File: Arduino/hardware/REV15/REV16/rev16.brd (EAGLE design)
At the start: 50 x 50 mm, 10 parts, among them U1 TC1185SMD

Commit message: up to rev18 cleaned up
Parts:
- moved - 34.7 mm to (48.6, 32.2), turned to 0 degrees
- moved + 34.2 mm to (48.6, 19.4), turned to 0 degrees
- moved U$2 27.9 mm to (-9.03, 25.8)
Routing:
- net VCC: track 68.2 -> 42.2 mm
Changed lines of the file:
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@@
 <plain>
 <text x="-5.318971875" y="13.33876875" size="1" layer="25" font="vector" rot="R180">20151208</text>
-<text x="24.149196875" y="-4.224378125" size="1" layer="22" font="vector" rot="MR0">License: http://goo.gl/3d71UJ</text>
-<text x="12.333878125" y="-0.70546875" size="1" layer="25" font="vector" rot="R180">OpenTRV.org.uk</text>
-<text x="2.54" y="24.13" size="1" layer="25" rot="R270">Remove jumper
+<text x="13.950803125" y="1.684378125" size="1" layer="22" font="vector" rot="MR180">License: http://goo.gl/3d71UJ</text>
+<text x="19.416121875" y="0.70546875" size="1" layer="25" font="vector">OpenTRV.org.uk</text>
+<text x="2.54" y="24.13" size="1" layer="25" font="vector" rot="R270">Remove jumper
 if battery power</text>
 <wire x1="0" y1="0" x2="0" y2="50" width="0.4064" layer="20"/>
@@
 <wire x1="50" y1="50" x2="50" y2="0" width="0.4064" layer="20"/>
 <wire x1="50" y1="0" x2="0" y2="0" width="0.4064" layer="20"/>
-<hole x="25.37" y="18.585" drill="2.8"/>
+<hole x="31.58" y="25.37" drill="2.8"/>
 </plain>
 <attributes>
@@
 </autorouter>
 <elements>
-<element name="U$2" library="logo" package="TONNE" value="" x="-9.025" y="53.75711875"/>
+<element name="U$2" library="logo" package="TONNE" value="" x="-9.025" y="25.81711875"/>
 <element name="U$1" library="ohw-logo" package="OSHW_10X200_NOTEXT" value="" x="-10.725834375" y="16.02610625"/>
-<element name="-" library="wirepad" package="2,15/1,0" value="" x="32.17" y="1.585" rot="R270"/>
-<element name="+" library="wirepad" package="2,15/1,0" value="" x="19.37" y="1.585" rot="R270"/>
+<element name="-" library="wirepad" package="2,15/1,0" value="" x="48.58" y="32.17"/>
+<element name="+" library="wirepad" package="2,15/1,0" value="" x="48.58" y="19.37"/>
 <element name="USBPOWER" library="micro-usb-fci-10103592" package="MICRO-USB-FCI-10103592" value="MICRO-USB-FCI-10103592" x="3.2" y="34.401771875" rot="MR90"/>
 <element name="I2C_EXT" library="pinhead" package="2X10" value="" x="18.05" y="45.905" smashed="yes">
-<attribute name="NAME" x="23.13" y="41.46" size="1.27" layer="25" ratio="10"/>
+<attribute name="NAME" x="23.13" y="41.46" size="1" layer="25" font="vector"/>
 <attribute name="VALUE" x="5.35" y="41.46" size="1.27" layer="27"/>
 </element>
 <element name="C1" library="SparkFun-Passives" package="0603-CAP" value="10uF 10V" x="11.43" y="31.75" smashed="yes" rot="R180">
-<attribute name="NAME" x="12.954" y="30.353" size="0.4064" layer="25" font="vector" rot="R180"/>
+<attribute name="NAME" x="15.494" y="32.258" size="1" layer="25" font="vector" rot="R180"/>
 </element>
 <element name="C2" library="SparkFun-Passives" package="0603-CAP" value="10uF 10V" x="11.43" y="41.275" smashed="yes" rot="R180">
-<attribute name="NAME" x="12.954" y="39.878" size="0.4064" layer="25" font="vector" rot="R180"/>
+<attribute name="NAME" x="15.494" y="41.783" size="1" layer="25" font="vector" rot="R180"/>
 </element>
 <element name="U1" library="3.3VREG" package="TC1185" value="TC1185SMD" x="11.43" y="36.83" smashed="yes">
-<attribute name="NAME" x="13.589" y="37.084" size="0.4064" layer="25" rot="R270"/>
-</element>
-<element name="JP1" library="jumper" package="JP1" value="" x="3.81" y="27.94"/>
+<attribute name="NAME" x="13.589" y="37.719" size="1" layer="25" font="vector" rot="R270"/>
+</element>
+<element name="JP1" library="jumper" package="JP1" value="" x="3.81" y="27.94" smashed="yes">
+<attribute name="NAME" x="7.112" y="26.67" size="1" layer="25" font="vector" rot="R90"/>
+<attribute name="VALUE" x="6.858" y="25.4" size="1.27" layer="27" ratio="10" rot="R90"/>
+</element>
 </elements>
 <signals>
@@
 <contactref element="JP1" pad="2"/>
 <wire x1="4.572" y1="29.1592" x2="3.8608" y2="29.1592" width="0.4064" layer="1"/>
-<wire x1="17.8816" y1="15.8496" x2="8.4328" y2="25.2984" width="0.4064" layer="1"/>
+<wire x1="34.3154" y1="17.8816" x2="8.4328" y2="25.2984" width="0" layer="19" extent="1-16"/>
 <wire x1="8.4328" y1="25.2984" x2="4.572" y2="29.1592" width="0.4064" layer="1"/>
-<wire x1="17.8816" y1="3.1496" x2="17.8816" y2="15.8496" width="0.4064" layer="1"/>
-<wire x1="19.4056" y1="1.6256" x2="17.8816" y2="3.1496" width="0.4064" layer="1"/>
+<wire x1="47.0154" y1="17.8816" x2="34.3154" y2="17.8816" width="0" layer="19" extent="1-16"/>
+<wire x1="48.5394" y1="19.4056" x2="47.0154" y2="17.8816" width="0.4064" layer="1"/>
 <wire x1="3.8608" y1="29.1592" x2="3.81" y2="29.21" width="0.4064" layer="1"/>
-<wire x1="19.4056" y1="1.6256" x2="19.37" y2="1.585" width="0.4064" layer="1"/>
+<wire x1="48.5394" y1="19.4056" x2="48.58" y2="19.37" width="0.4064" layer="1"/>
 <wire x1="6.096" y1="47.1424" x2="6.604" y2="47.1424" width="0.4064" layer="1"/>
 <wire x1="4.7752" y1="45.8216" x2="6.096" y2="47.1424" width="0.4064" layer="1"/>

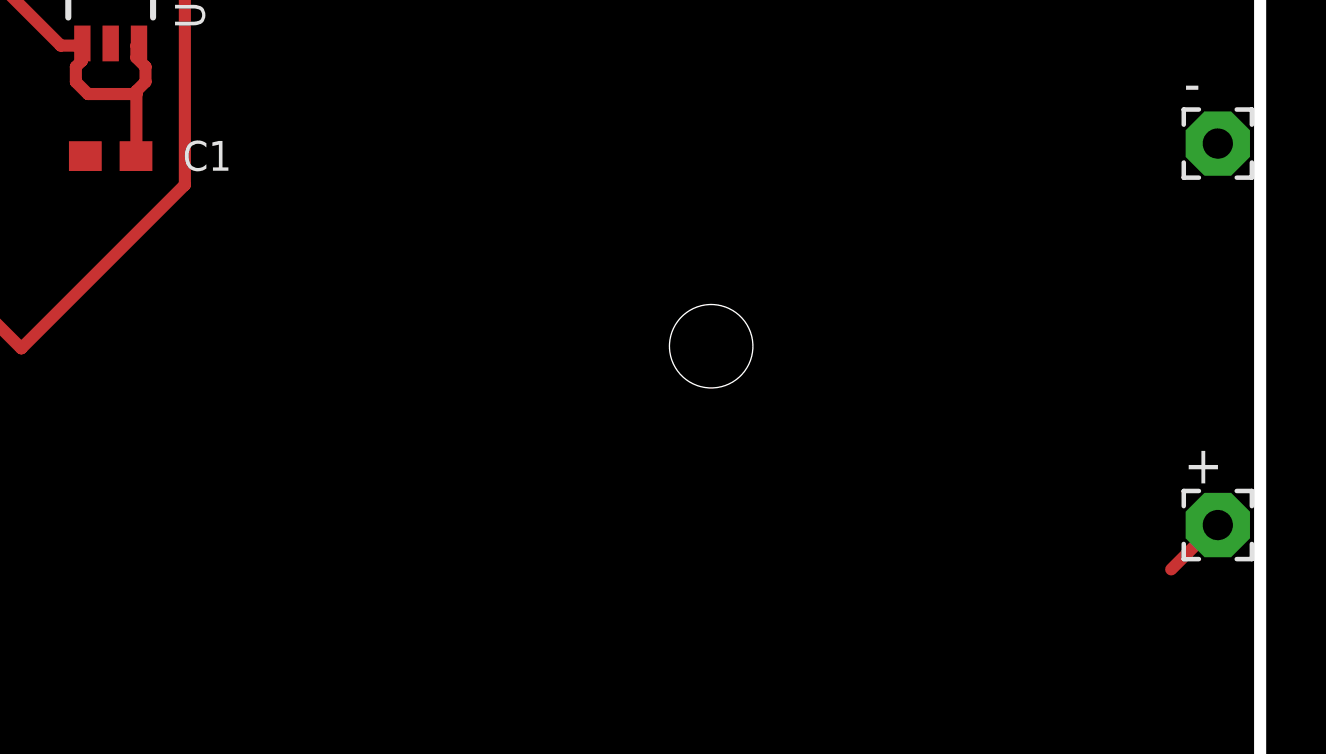
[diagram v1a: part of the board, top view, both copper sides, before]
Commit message: up to rev18 DRC check and ground plane
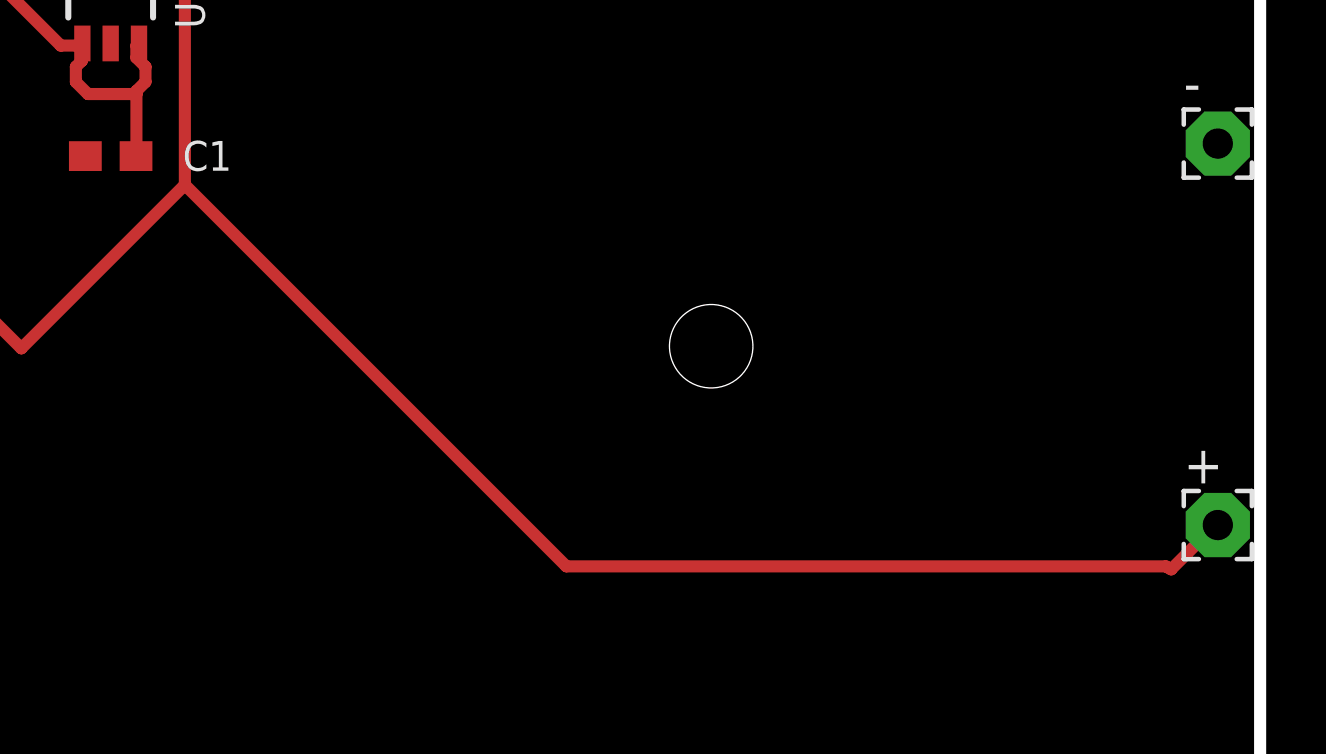
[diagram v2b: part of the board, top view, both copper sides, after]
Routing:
- net VCC: track 42.2 -> 80.6 mm
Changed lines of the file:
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@@
 <contactref element="JP1" pad="2"/>
 <wire x1="4.572" y1="29.1592" x2="3.8608" y2="29.1592" width="0.4064" layer="1"/>
-<wire x1="34.3154" y1="17.8816" x2="8.4328" y2="25.2984" width="0" layer="19" extent="1-16"/>
 <wire x1="8.4328" y1="25.2984" x2="4.572" y2="29.1592" width="0.4064" layer="1"/>
-<wire x1="47.0154" y1="17.8816" x2="34.3154" y2="17.8816" width="0" layer="19" extent="1-16"/>
 <wire x1="48.5394" y1="19.4056" x2="47.0154" y2="17.8816" width="0.4064" layer="1"/>
 <wire x1="3.8608" y1="29.1592" x2="3.81" y2="29.21" width="0.4064" layer="1"/>
@@
 <wire x1="8.4328" y1="25.2984" x2="13.9192" y2="30.7848" width="0.4064" layer="1"/>
 <wire x1="6.604" y1="47.1424" x2="6.62" y2="47.175" width="0.4064" layer="1"/>
+<wire x1="26.7208" y1="17.9832" x2="46.8376" y2="17.9832" width="0.4064" layer="1"/>
+<wire x1="13.9192" y1="30.7848" x2="26.7208" y2="17.9832" width="0.4064" layer="1"/>
+<wire x1="46.8376" y1="17.9832" x2="47.0154" y2="17.8816" width="0.4064" layer="1"/>
 </signal>
 <signal name="GND" class="1">

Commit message: REV15-18 cleaned up, need sanity check
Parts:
- moved U$2 47.6 mm to (38.0, 33.4)
- moved U$1 24.1 mm to (12.1, 8.41)
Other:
- board text added: "20160229"
- board text removed: "20151208"
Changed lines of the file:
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@@
 <board>
 <plain>
-<text x="-5.318971875" y="13.33876875" size="1" layer="25" font="vector" rot="R180">20151208</text>
+<text x="47.62123125" y="13.731028125" size="1" layer="25" font="vector" rot="R270">20160229</text>
 <text x="13.950803125" y="1.684378125" size="1" layer="22" font="vector" rot="MR180">License: http://goo.gl/3d71UJ</text>
 <text x="19.416121875" y="0.70546875" size="1" layer="25" font="vector">OpenTRV.org.uk</text>
@@
 </autorouter>
 <elements>
-<element name="U$2" library="logo" package="TONNE" value="" x="-9.025" y="25.81711875"/>
-<element name="U$1" library="ohw-logo" package="OSHW_10X200_NOTEXT" value="" x="-10.725834375" y="16.02610625"/>
+<element name="U$2" library="logo" package="TONNE" value="" x="37.965" y="33.43711875"/>
+<element name="U$1" library="ohw-logo" package="OSHW_10X200_NOTEXT" value="" x="12.134165625" y="8.40610625"/>
 <element name="-" library="wirepad" package="2,15/1,0" value="" x="48.58" y="32.17"/>
 <element name="+" library="wirepad" package="2,15/1,0" value="" x="48.58" y="19.37"/>

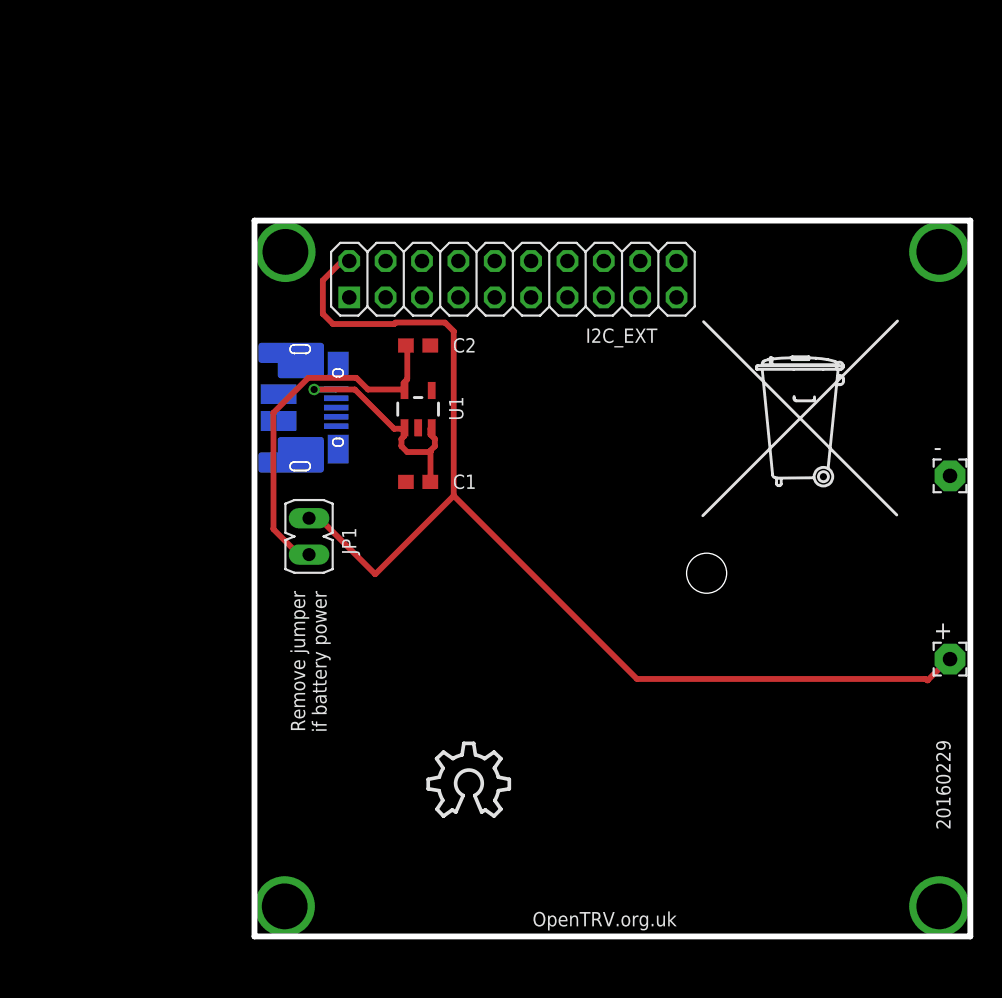
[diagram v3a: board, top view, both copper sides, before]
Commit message: rev15-18 changed as per Deniz suggeastions
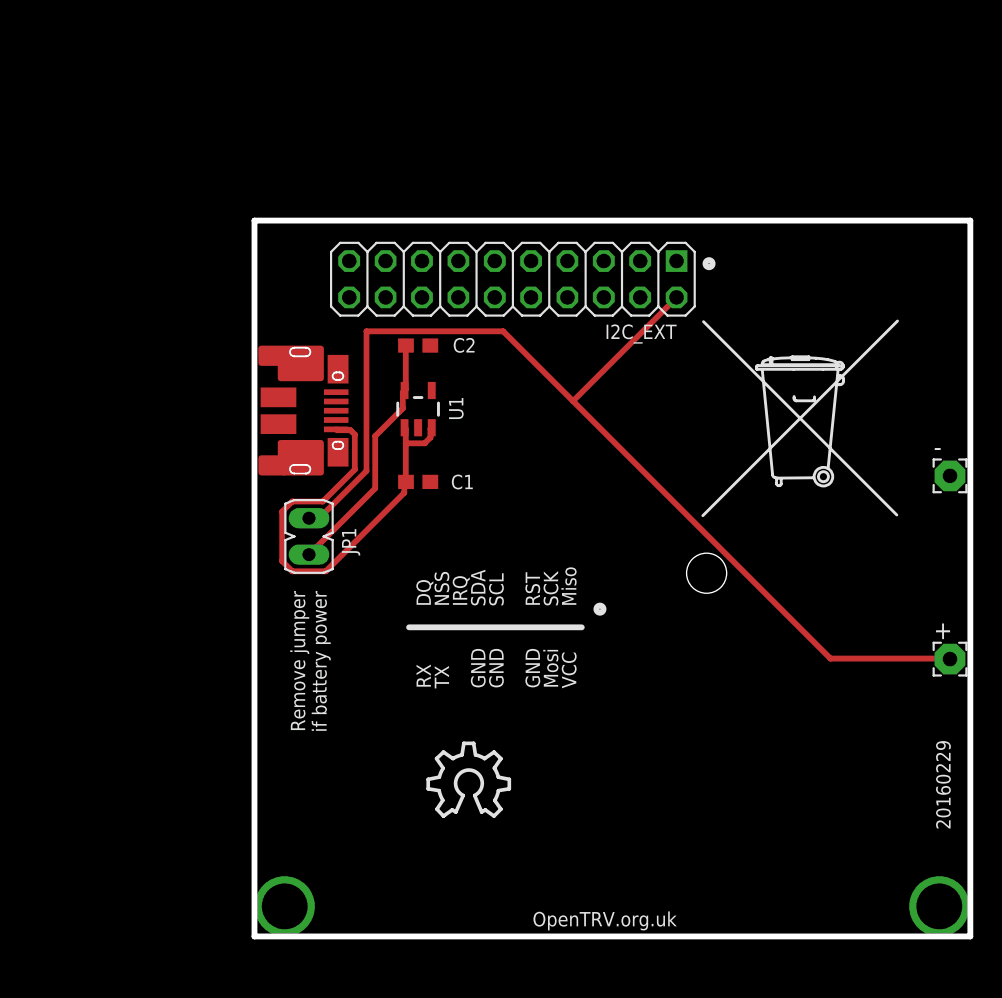
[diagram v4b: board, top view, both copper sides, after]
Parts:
- moved USBPOWER 4.86 mm to (3.20, 39.3), flipped to the top, turned to 270 degrees
- turned C1 to 0 degrees
- turned I2C_EXT to 180 degrees
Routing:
- net 5V: track 16.7 -> 32.0 mm, vias 1 -> 0
- net N$8: track 25.2 -> 17.4 mm
- net VCC: track 80.6 -> 75.6 mm
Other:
- board text added: "DQ"
- board text added: "GND"
- board text added: "IRQ"
- board text added: "Miso"
- board text added: "Mosi"
- board text added: "NSS"
- board text added: "RST"
- board text added: "RX"
- board text added: "SCK"
- board text added: "SCL"
- board text added: "SDA"
- board text added: "TX"
- board text added: "VCC"

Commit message: ic2_ext labels closer to connector
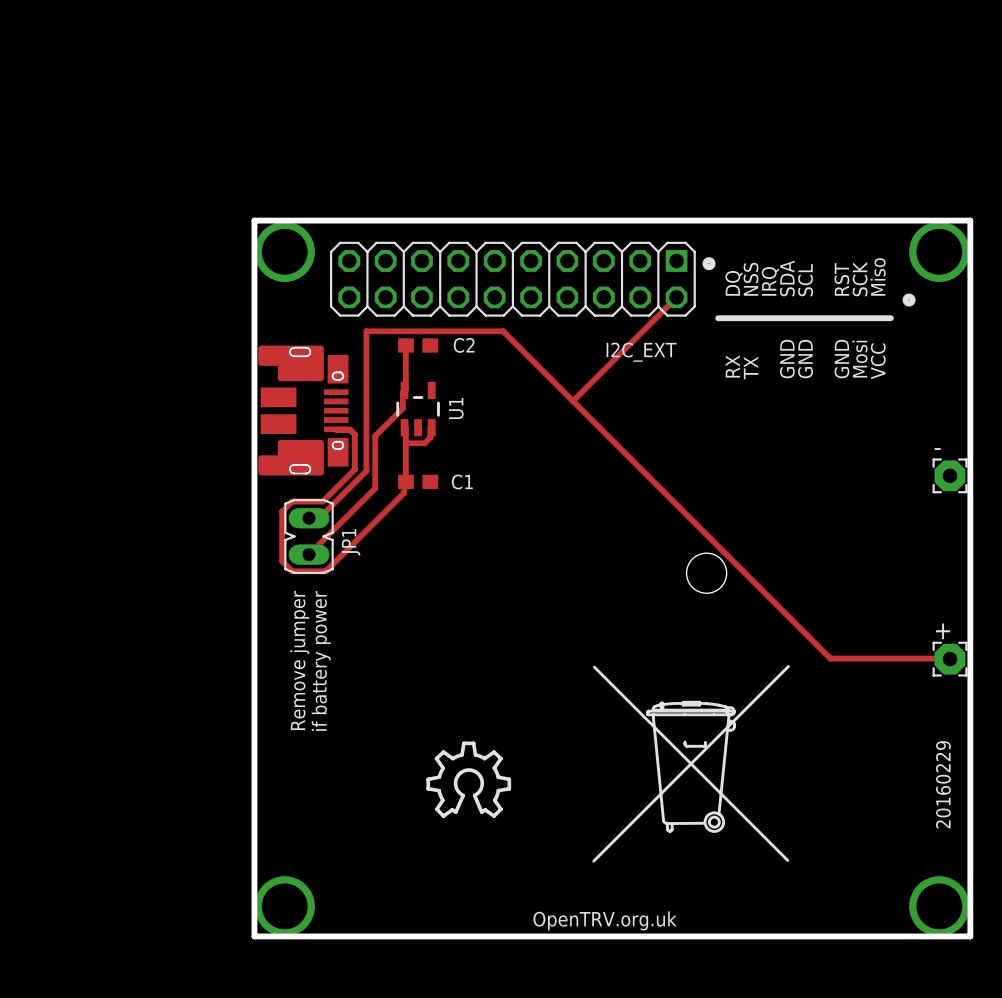
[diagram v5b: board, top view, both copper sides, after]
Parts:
- moved U$2 25.3 mm to (30.3, 9.31)
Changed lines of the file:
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@@
 <wire x1="50" y1="0" x2="0" y2="0" width="0.4064" layer="20"/>
 <hole x="31.58" y="25.37" drill="2.8"/>
-<text x="12.32" y="23.04" size="1" layer="25" rot="R90">DQ</text>
-<text x="16.13" y="23.04" size="1" layer="25" rot="R90">SDA</text>
-<text x="22.48" y="23.04" size="1" layer="25" rot="R90">Miso</text>
-<text x="22.48" y="17.325" size="1" layer="25" rot="R90">VCC</text>
-<text x="21.21" y="23.04" size="1" layer="25" rot="R90">SCK</text>
-<text x="21.21" y="17.325" size="1" layer="25" rot="R90">Mosi</text>
-<text x="19.94" y="23.04" size="1" layer="25" rot="R90">RST</text>
-<text x="19.94" y="17.325" size="1" layer="25" rot="R90">GND</text>
-<text x="14.86" y="23.04" size="1" layer="25" rot="R90">IRQ</text>
-<text x="13.59" y="23.04" size="1" layer="25" rot="R90">NSS</text>
-<text x="12.32" y="17.325" size="1" layer="25" rot="R90">RX</text>
-<text x="17.4" y="23.04" size="1" layer="25" rot="R90">SCL</text>
-<text x="13.59" y="17.325" size="1" layer="25" rot="R90">TX</text>
-<wire x1="22.86" y1="21.59" x2="10.795" y2="21.59" width="0.4064" layer="25"/>
-<text x="17.4" y="17.325" size="1" layer="25" rot="R90">GND</text>
-<text x="16.13" y="17.325" size="1" layer="25" rot="R90">GND</text>
-<circle x="24.13" y="22.86" radius="0.25" width="0.4064" layer="25"/>
+<text x="33.91" y="44.63" size="1" layer="25" rot="R90">DQ</text>
+<text x="37.72" y="44.63" size="1" layer="25" rot="R90">SDA</text>
+<text x="44.07" y="44.63" size="1" layer="25" rot="R90">Miso</text>
+<text x="44.07" y="38.915" size="1" layer="25" rot="R90">VCC</text>
+<text x="42.8" y="44.63" size="1" layer="25" rot="R90">SCK</text>
+<text x="42.8" y="38.915" size="1" layer="25" rot="R90">Mosi</text>
+<text x="41.53" y="44.63" size="1" layer="25" rot="R90">RST</text>
+<text x="41.53" y="38.915" size="1" layer="25" rot="R90">GND</text>
+<text x="36.45" y="44.63" size="1" layer="25" rot="R90">IRQ</text>
+<text x="35.18" y="44.63" size="1" layer="25" rot="R90">NSS</text>
+<text x="33.91" y="38.915" size="1" layer="25" rot="R90">RX</text>
+<text x="38.99" y="44.63" size="1" layer="25" rot="R90">SCL</text>
+<text x="35.18" y="38.915" size="1" layer="25" rot="R90">TX</text>
+<wire x1="44.45" y1="43.18" x2="32.385" y2="43.18" width="0.4064" layer="25"/>
+<text x="38.99" y="38.915" size="1" layer="25" rot="R90">GND</text>
+<text x="37.72" y="38.915" size="1" layer="25" rot="R90">GND</text>
+<circle x="45.72" y="44.45" radius="0.25" width="0.4064" layer="25"/>
 <circle x="31.75" y="46.99" radius="0.25" width="0.4064" layer="25"/>
 </plain>
@@
 </autorouter>
 <elements>
-<element name="U$2" library="logo" package="TONNE" value="" x="37.965" y="33.43711875"/>
+<element name="U$2" library="logo" package="TONNE" value="" x="30.345" y="9.30711875"/>
 <element name="U$1" library="ohw-logo" package="OSHW_10X200_NOTEXT" value="" x="12.134165625" y="8.40610625"/>
 <element name="-" library="wirepad" package="2,15/1,0" value="" x="48.58" y="32.17"/>
@@
 <element name="USBPOWER" library="micro-usb-fci-10103592" package="MICRO-USB-FCI-10103592" value="MICRO-USB-FCI-10103592" x="3.2" y="39.258228125" rot="R270"/>
 <element name="I2C_EXT" library="pinhead" package="2X10" value="" x="18.05" y="45.905" smashed="yes" rot="R180">
-<attribute name="NAME" x="29.48" y="42.73" size="1" layer="25" font="vector" rot="R180"/>
+<attribute name="NAME" x="29.48" y="41.46" size="1" layer="25" font="vector" rot="R180"/>
 <attribute name="VALUE" x="30.75" y="50.35" size="1.27" layer="27" rot="R180"/>
 </element>
@@
 <wire x1="10.3632" y1="37.9984" x2="10.48" y2="38.1301" width="0.4064" layer="1"/>
 </signal>
+<signal name="GND1" class="1">
+<via x="47.832378125" y="47.8194875" extent="1-16" drill="3.2"/>
+<via x="2.112378125" y="47.8194875" extent="1-16" drill="3.2"/>
+</signal>
 </signals>
